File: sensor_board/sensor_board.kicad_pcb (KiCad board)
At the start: 2 copper layers, 102.2 x 39.9 mm, 49 parts, among them J1 zigbee connector, J2 SWD, J3 USB_B_Micro, J4 AM2320, J5 Lithium_battery_conn, J6 ACC, U1 MCP6002-xMC, U2 MIC5365-3.3YC5, U3 STM32L051C8Tx, U4 MIC5365-3.3YC5, U5 SDC42

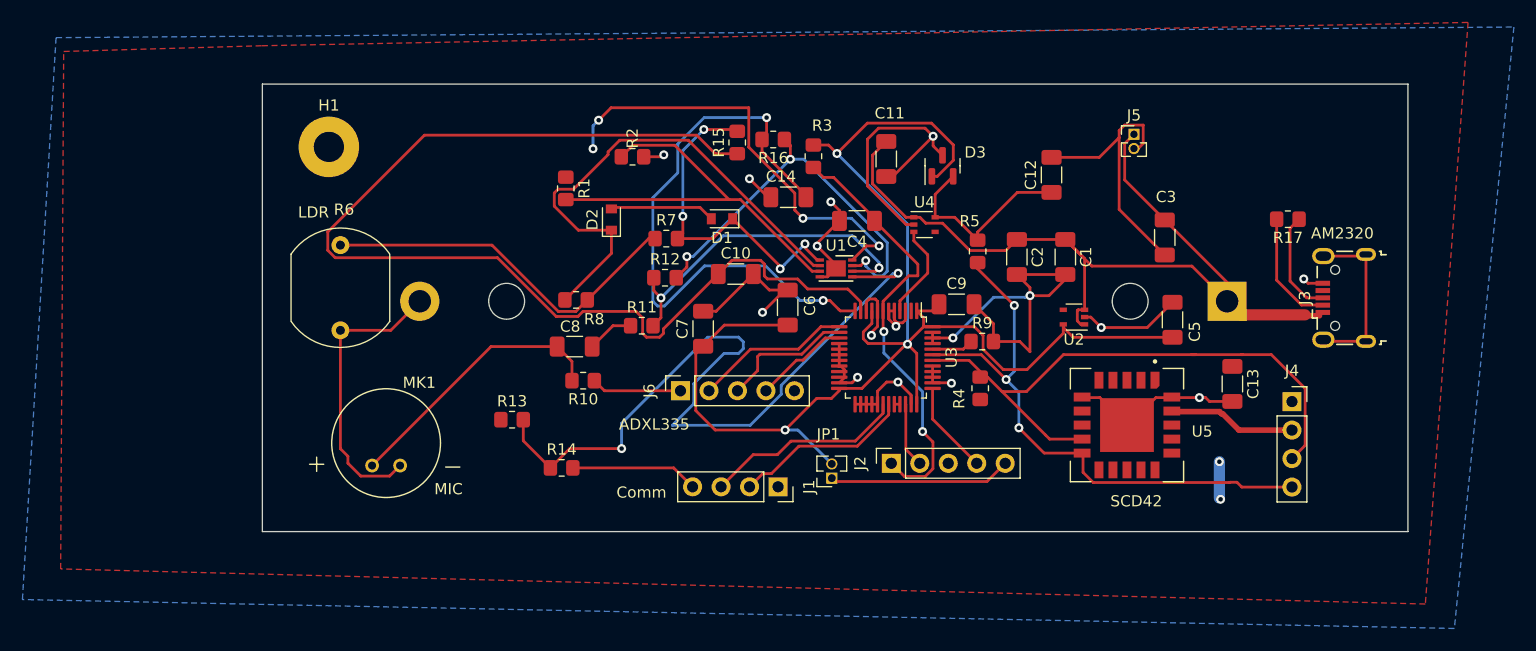
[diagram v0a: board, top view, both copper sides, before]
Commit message: add reverse polarity protection mosfet and diode
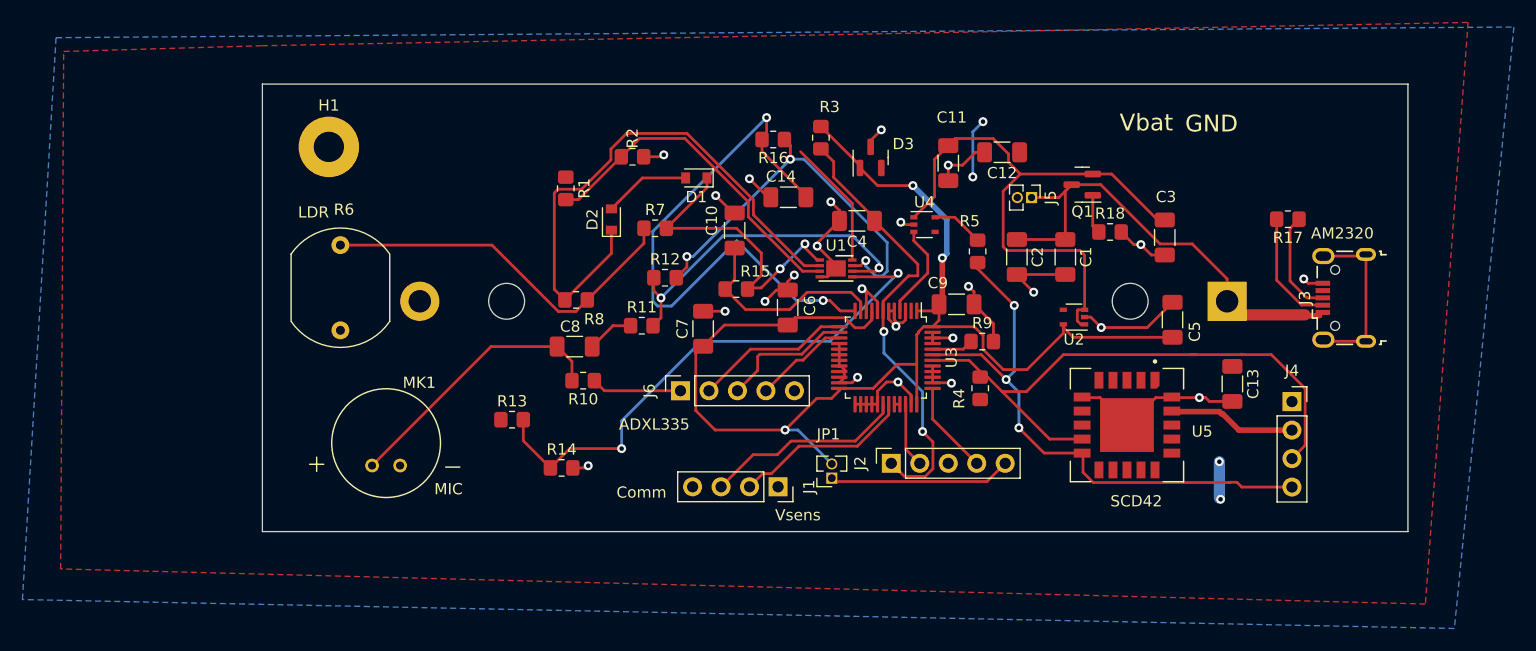
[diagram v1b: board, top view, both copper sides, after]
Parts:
- added Q1: DMP3098LQ, Package_TO_SOT_SMD:SOT-23, F.Cu at (178.1, 68.2)
- added R18: 10k, Resistor_SMD:R_0805_2012Metric_Pad1.20x1.40mm_HandSolder, F.Cu at (180.6, 72.5)
- moved R15 13.1 mm to (147.3, 77.6), turned to 0 degrees
- moved J5 10.7 mm to (173.6, 69.4), turned to -90 degrees
- moved D3 6.45 mm to (159.3, 65.8)
- moved C11 5.54 mm to (166.2, 66.3)
- moved C12 4.85 mm to (171.0, 65.4), turned to 180 degrees
- moved D1 4.30 mm to (143.7, 67.7)
- moved C10 3.88 mm to (147.1, 72.3), turned to 90 degrees
- moved R3 1.78 mm to (154.8, 64.1)
- moved R7 1.35 mm to (140.1, 72.1)
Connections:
- C11 pad 1: V_bat -> 5V
- C3 pad 1: V_bat -> 5V
- U2 pad 1: V_bat -> 5V
- U2 pad 3: V_bat -> 5V
- U4 pad 1: V_bat -> 5V
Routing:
- net GND: track 200.8 -> 104.8 mm, vias 16 -> 24
- net Vpr: track 100.4 -> 18.6 mm
- net 5V: track 0.00 -> 52.4 mm
- net V_bat: track 78.6 -> 42.0 mm
- net 3.3V_SENS: track 79.7 -> 44.3 mm, vias 6 -> 4
- net Net-(R13-Pad2): track 70.1 -> 49.2 mm
- net 3.3V: track 126.5 -> 113.5 mm
- net Net-(R1-Pad2): track 37.3 -> 30.6 mm
- net Net-(D2-Pad1): track 45.5 -> 50.0 mm
- net Net-(Q1-Pad1): track 0.00 -> 3.49 mm
- net Net-(D1-Pad1): track 30.9 -> 28.5 mm, vias 4 -> 2
- net Net-(D1-Pad2): track 9.38 -> 7.76 mm
- net MIC: track 54.1 -> 52.7 mm
- net NRST: track 39.4 -> 40.2 mm
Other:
- board text added: "GND"
- board text added: "Vbat"
- board text added: "Vsens"

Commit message: add testpoints
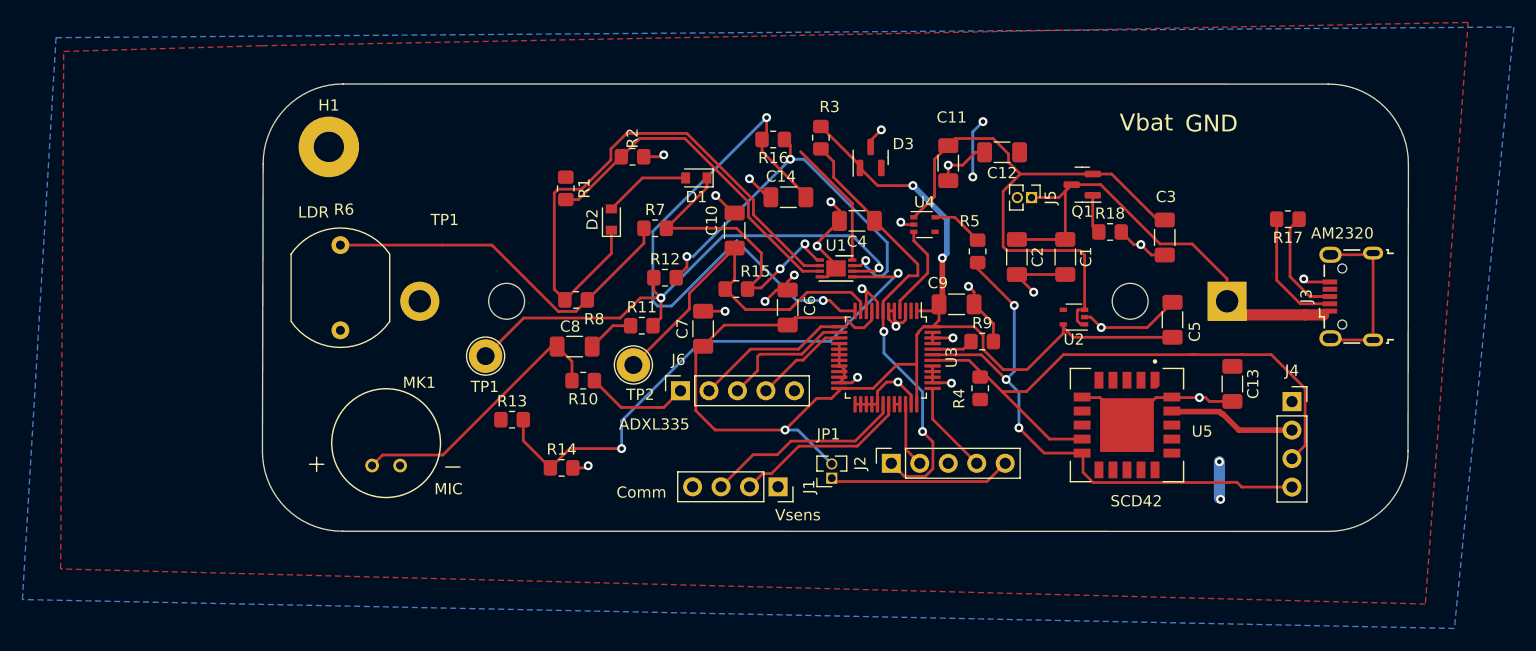
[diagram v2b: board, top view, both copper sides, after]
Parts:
- added TP1: TestPoint, TestPoint:TestPoint_Loop_D2.60mm_Drill1.6mm_Beaded, F.Cu at (124.9, 83.5)
- added TP2: TestPoint, TestPoint:TestPoint_Loop_D2.60mm_Drill1.6mm_Beaded, F.Cu at (138.1, 84.3)
- moved J3 0.65 mm to (202.1, 78.2)
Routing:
- net Net-(R11-Pad2): track 30.6 -> 48.4 mm
- net Vpr: track 18.6 -> 32.8 mm
- net 3.3V_SENS: track 44.3 -> 45.5 mm
- net Net-(J3-Pad2): track 10.5 -> 11.1 mm
- net GND: track 104.8 -> 105.4 mm
- net Net-(J3-Pad3): track 9.40 -> 9.97 mm
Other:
- outline, holes or cut-outs redrawn
- board text added: "TP1"

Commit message: add cap to ..
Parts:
- added C15: 0.1u, Capacitor_SMD:C_1206_3216Metric_Pad1.33x1.80mm_HandSolder, F.Cu at (138.1, 92.2)
- added C16: 0.1u, Capacitor_SMD:C_1206_3216Metric_Pad1.33x1.80mm_HandSolder, F.Cu at (144.2, 90.7)
- added C17: 0.1u, Capacitor_SMD:C_1206_3216Metric_Pad1.33x1.80mm_HandSolder, F.Cu at (149.8, 90.3)
- added J7: DBG_PWR, TerminalBlock:TerminalBlock_bornier-2_P5.08mm, F.Cu at (187.8, 63.2)
- added R19: 470, Resistor_SMD:R_0805_2012Metric_Pad1.20x1.40mm_HandSolder, F.Cu at (167.6, 90.5)
- added R20: 470, Resistor_SMD:R_0805_2012Metric_Pad1.20x1.40mm_HandSolder, F.Cu at (163.4, 91.9)
- J1: value zigbee connector -> zigbee
- moved J2 2.17 mm to (161.7, 95.2)
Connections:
- J2 pad 2: SWDIO -> Net-(J2-Pad2)
- J2 pad 4: SWCLK -> Net-(J2-Pad4)
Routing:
- net Net-(D2-Pad1): track 50.0 -> 34.5 mm, vias 0 -> 2
- net GND: track 105.4 -> 117.1 mm
- net 5V: track 52.4 -> 63.7 mm
- net Gx: track 14.0 -> 21.9 mm
- net 3.3V: track 113.5 -> 107.3 mm, vias 3 -> 5
- net Net-(J2-Pad4): track 0.00 -> 4.99 mm
- net Gy: track 12.0 -> 16.7 mm
- net Gz: track 8.49 -> 12.9 mm
- net Net-(J2-Pad2): track 0.00 -> 3.29 mm
- net SWCLK: track 8.31 -> 5.09 mm
- net Net-(J2-Pad5): track 16.3 -> 19.3 mm
- net NRST: track 40.2 -> 37.8 mm, vias 2 -> 1
- net SWDIO: track 5.79 -> 4.03 mm
